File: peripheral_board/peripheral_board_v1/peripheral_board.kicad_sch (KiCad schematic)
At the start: 0 parts

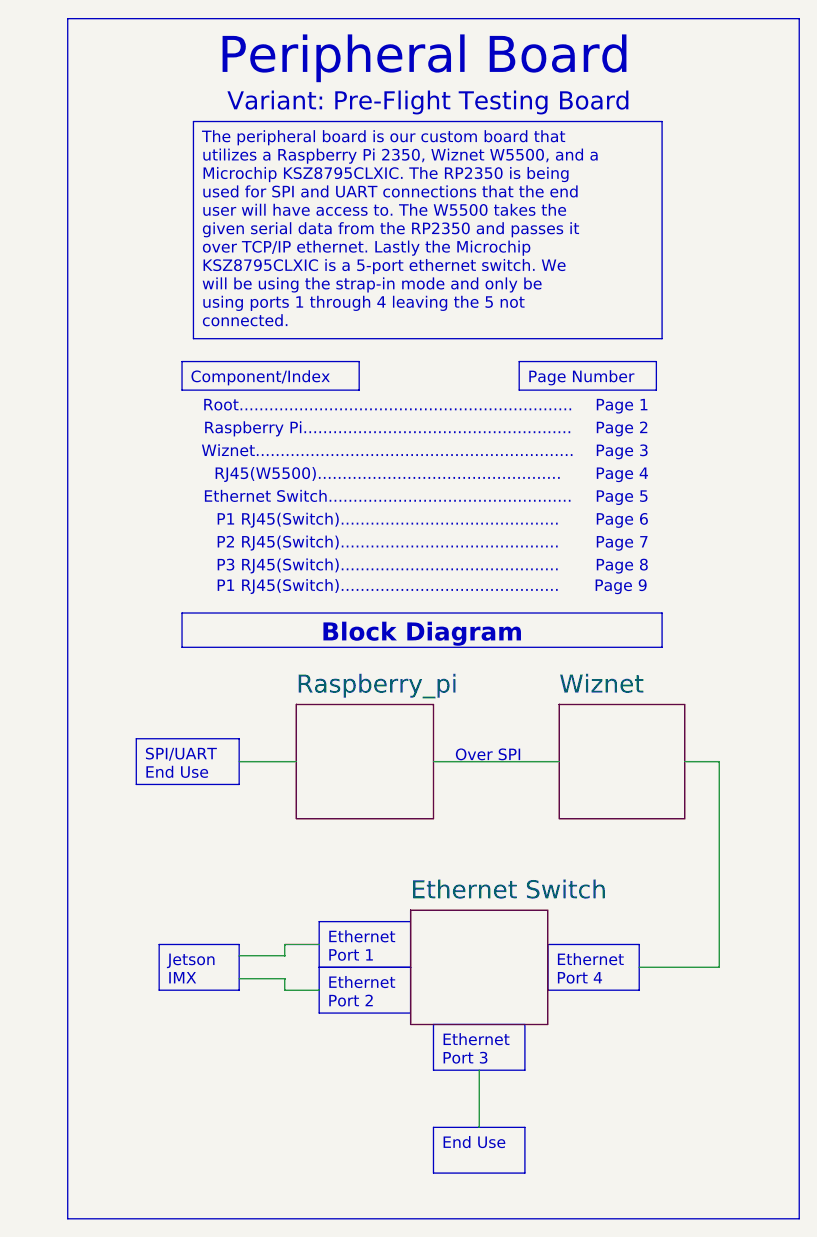
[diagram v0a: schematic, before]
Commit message: Update to the PCB
#Changes made so far

## Wiznet
* Changed the Wiznet layout to match that of their development board
* Restructured the RJ45 connections
    * *Looked over the RJ45 still a unsure*
    * Added in 2 differnt versions of Ethernt Connections. The one that shows the magnetics might be used for the Ethernet switch.
* Removed the Single Bus Buffer gate with 3-state output to match the dev board

## Raspberry Pi
* Moved to USB type C from micro USB for debugging.
* Changed the GPIO pins to match the Wiznet dev board.
* Brought in breakout pins for the rest of the GPIO.
* Cleaned up the Schematic to make it more clean.

## Ethernet Switch
* Changed the crystal to be the same as the Wiznet and to have the correct load caps
* Looking at the design check list to help get moving forward, need to relook at power distribution.
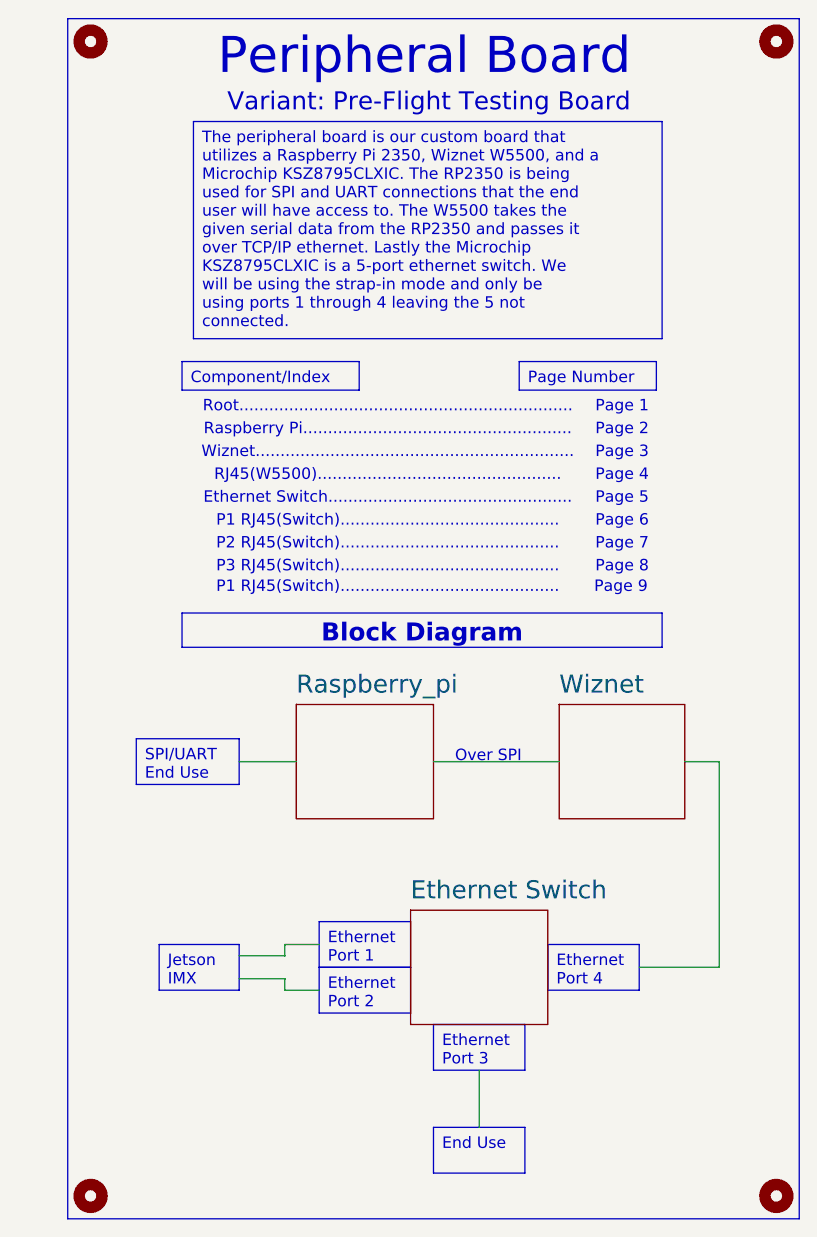
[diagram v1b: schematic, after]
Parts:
- added H1, H2, H3, H4: MountingHole, MountingHole:MountingHole_2.5mm_Pad, symbol Mechanical:MountingHole

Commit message: Schematic design ready for review
Made the last changes for the Wiznet by adding in Dip switches and made sure that the interrupt and reset signals are attached to the raspberry pi.

Finished the Etherent switch by wiring the RJ45 port 1 with 2 configurations, leaning more towards not using the Wiznet port but might do it any ways for cost. Added test points to port 5 but might change it to be RMII configuration because the 4 port strap in mode sets it to that config. Put solder jumpers in for the LED strap in mode. On the schematic I put in a note about how to configure to the proper mode we want but after a review will change to be a hardwire set. Made the reset switch match that of the EVAL board but further reading found I do not need the diode. Created the VDDIO and VDDAT which are just 2 different versions of 3.3V. Layout would be next but need to learn more about trace integrity and impedance control.
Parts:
- renumbered H4 to H1, H3 to H2, H1 to H3, H2 to H4
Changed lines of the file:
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@@
 		(on_board yes)
 		(dnp no)
-		(property "Reference" "H1"
+		(property "Reference" "H3"
 			(at 179.07 31.7499 0)
 			(effects
@@
 			(project "peripheral_board"
 				(path "/14f8712f-1710-40cb-b01e-cc9b3c4405bd"
-					(reference "H1")
+					(reference "H3")
 					(unit 1)
 				)
@@
 		(dnp no)
 		(fields_autoplaced yes)
-		(property "Reference" "H4"
+		(property "Reference" "H1"
 			(at 102.87 31.7499 0)
 			(effects
@@
 			(project "peripheral_board"
 				(path "/14f8712f-1710-40cb-b01e-cc9b3c4405bd"
-					(reference "H4")
+					(reference "H1")
 					(unit 1)
 				)
@@
 		(dnp no)
 		(fields_autoplaced yes)
-		(property "Reference" "H3"
+		(property "Reference" "H2"
 			(at 102.87 160.0199 0)
 			(effects
@@
 			(project "peripheral_board"
 				(path "/14f8712f-1710-40cb-b01e-cc9b3c4405bd"
-					(reference "H3")
+					(reference "H2")
 					(unit 1)
 				)
@@
 		(dnp no)
 		(fields_autoplaced yes)
-		(property "Reference" "H2"
+		(property "Reference" "H4"
 			(at 179.07 160.0199 0)
 			(effects
@@
 			(project "peripheral_board"
 				(path "/14f8712f-1710-40cb-b01e-cc9b3c4405bd"
-					(reference "H2")
-					(unit 1)
-				)
+					(reference "H4")
+					(unit 1)
+				)

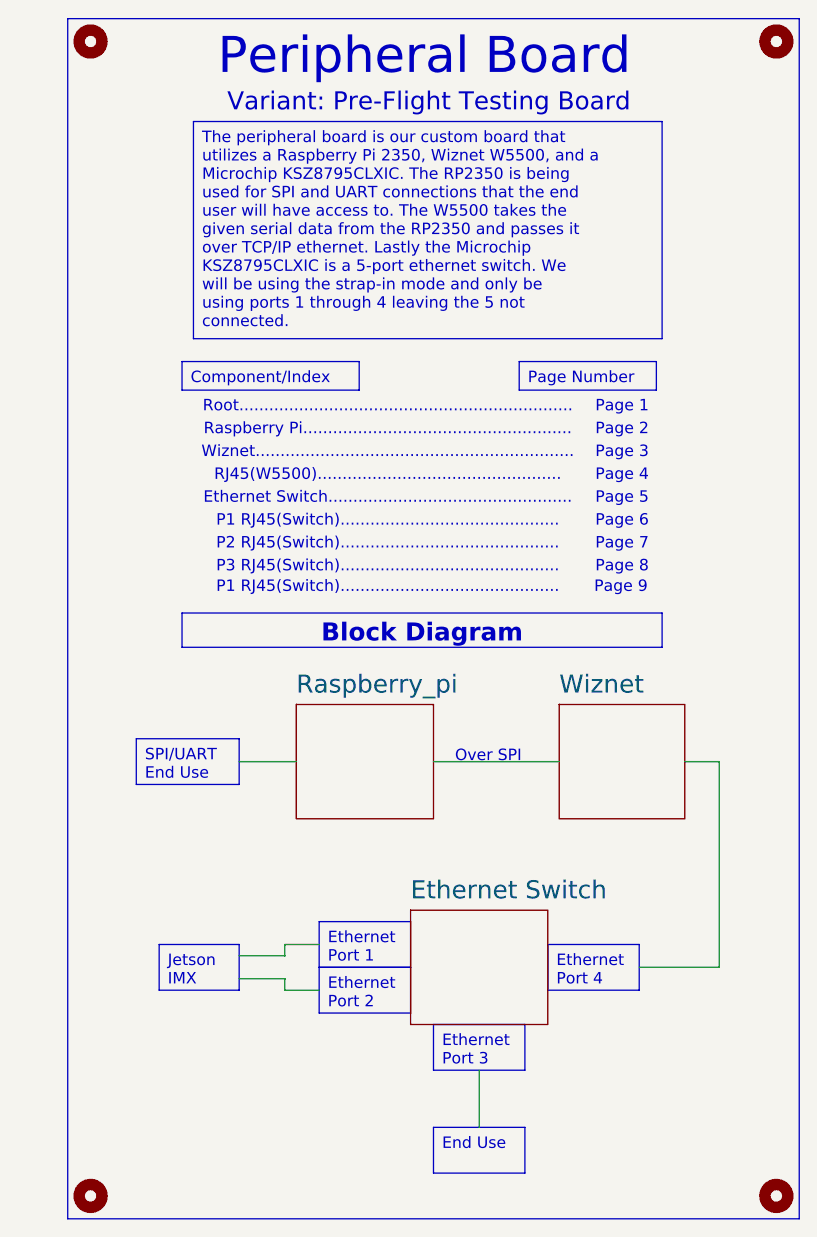
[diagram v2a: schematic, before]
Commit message: Started the PCB layout
Finished the schematic. Now working on the PCB. Might looking in to moving to a 6 layer board.
Need to do a bit of redesign because changing some of the parts had different footprints.

Started on the Wiznet and the its RJ45 port it has. Want to make the port close to the chip as a possible. Currently working on the 4 layer stack up but if I switch to a 6 layer it might help with impedance and change the overall signal layering.
Almost done with the Wiznet just need to do the clock and the TX/RX pairs.
Once that is done I will work on the Ethernet switch then lastly the breakout pins for the RP.

I should have selected either a 6 layer or 4 layer board, leaning more towards 6 layer because I can keep my signals separated by the 3 and 3 sections.
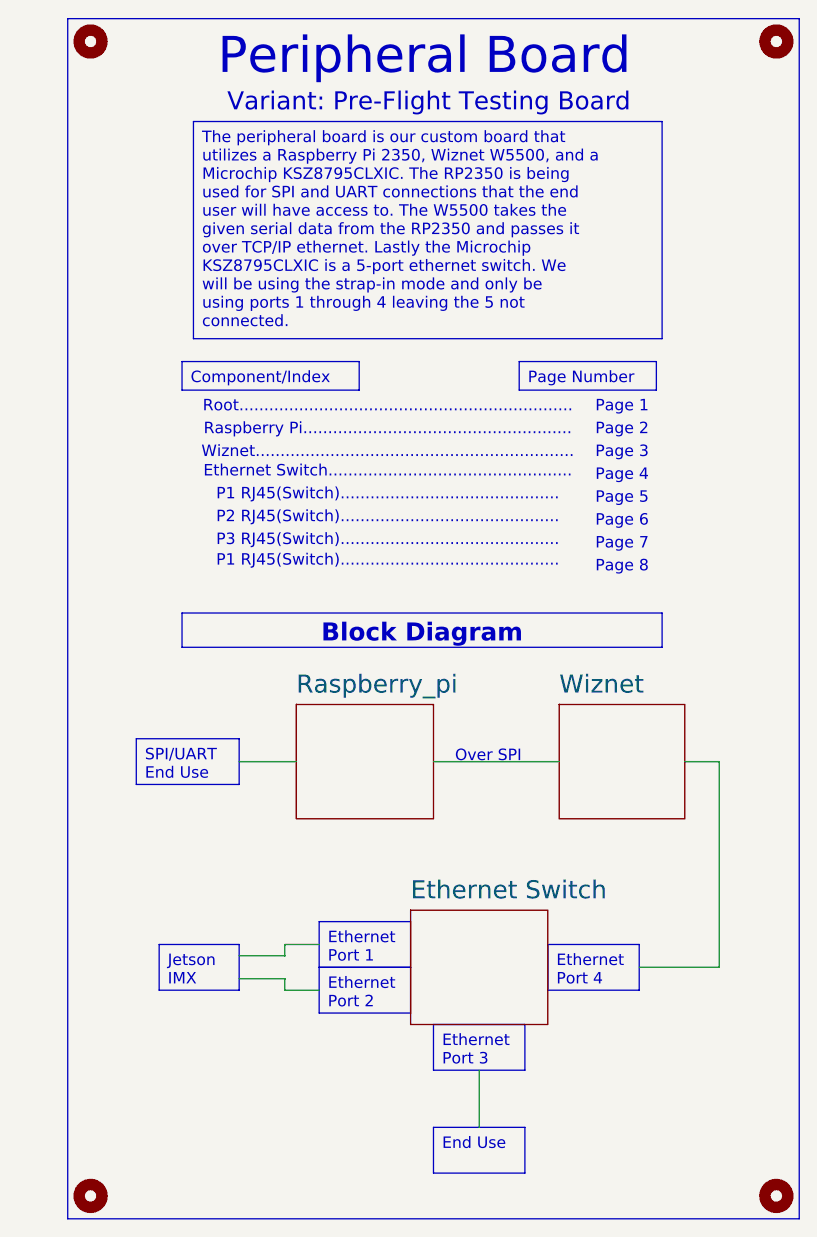
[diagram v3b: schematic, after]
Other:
- note removed: "Page 9"
- note removed: "RJ45(W5500)................................................."
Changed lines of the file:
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@@
 	(text "P3 RJ45(Switch)............................................\n"
 		(exclude_from_sim no)
-		(at 133.35 91.44 0)
+		(at 133.35 88.519 0)
 		(effects
 			(font
@@
 	(text "P1 RJ45(Switch)............................................\n"
 		(exclude_from_sim no)
-		(at 133.35 86.36 0)
-		(effects
-			(font
-				(size 1.27 1.27)
-			)
-		)
-	)
-	(text "RJ45(W5500).................................................\n"
-		(exclude_from_sim no)
-		(at 133.35 81.28 0)
+		(at 133.35 83.439 0)
 		(effects
 			(font
@@
 	(text "Ethernet Switch.................................................\n"
 		(exclude_from_sim no)
-		(at 133.35 83.82 0)
+		(at 133.35 80.899 0)
 		(effects
 			(font
@@
 	(text "P2 RJ45(Switch)............................................\n"
 		(exclude_from_sim no)
-		(at 133.35 88.9 0)
+		(at 133.35 85.979 0)
 		(effects
 			(font
@@
 	(text "P1 RJ45(Switch)............................................\n"
 		(exclude_from_sim no)
-		(at 133.35 93.726 0)
+		(at 133.35 90.805 0)
 		(effects
 			(font
@@
 				(thickness 0.254)
 			)
-		)
-	)
-	(text "Page 9"
-		(exclude_from_sim no)
-		(at 159.258 93.726 0)
-		(effects
-			(font
-				(size 1.27 1.27)
-			)
-			(href "#9")
 		)
 	)
@@
 			(project "peripheral_board"
 				(path "/14f8712f-1710-40cb-b01e-cc9b3c4405bd"
-					(page "5")
-				)
-			)
+					(page "4")
+				)
+			)
